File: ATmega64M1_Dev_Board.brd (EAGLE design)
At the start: 99.1 x 53.3 mm, 67 parts, among them IC1 LM1117IMPX-3.3, IC11 ATMEGA64M1TQFP32, IC2 LM1117IMPX-5.0, IC3 ADM3053M, IC4 FT232RL, J1 DCJ0202, Q1 16M, U1 MCP2562

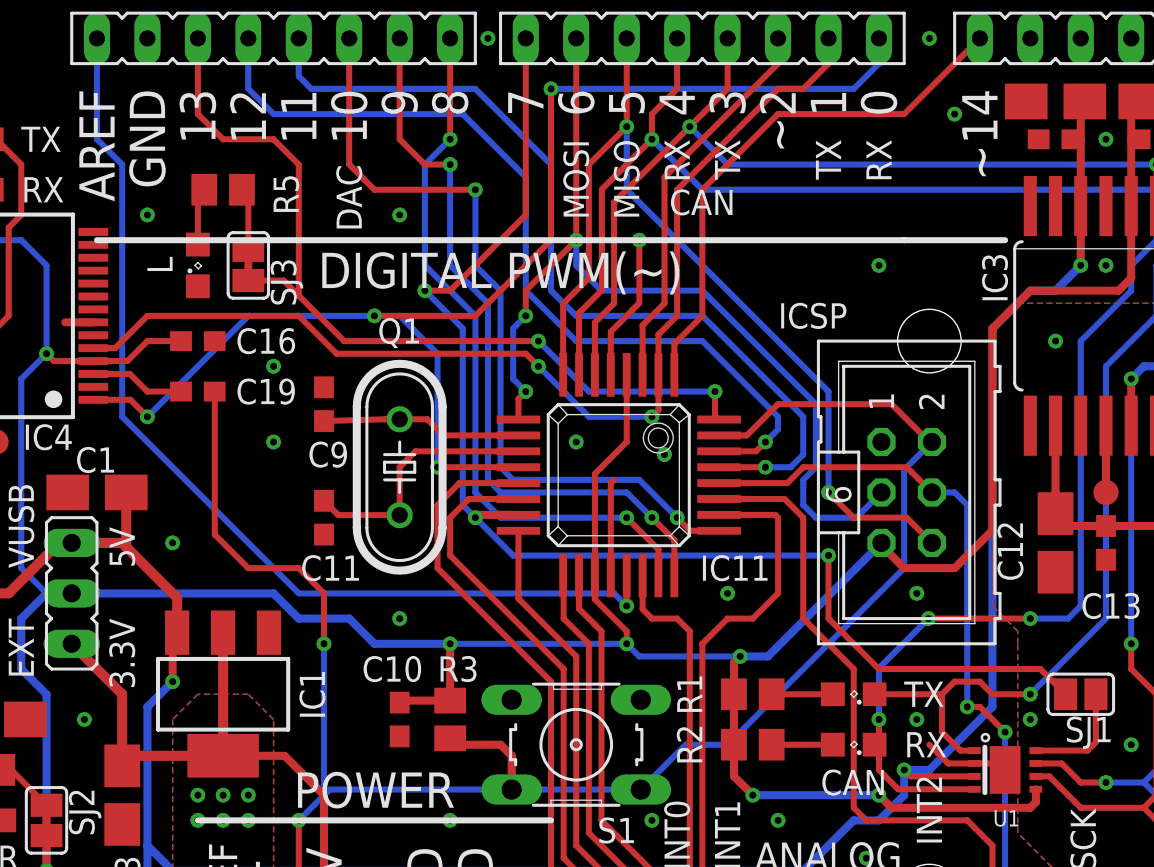
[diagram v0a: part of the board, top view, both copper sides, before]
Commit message: Fixed ICSP pin allocation.
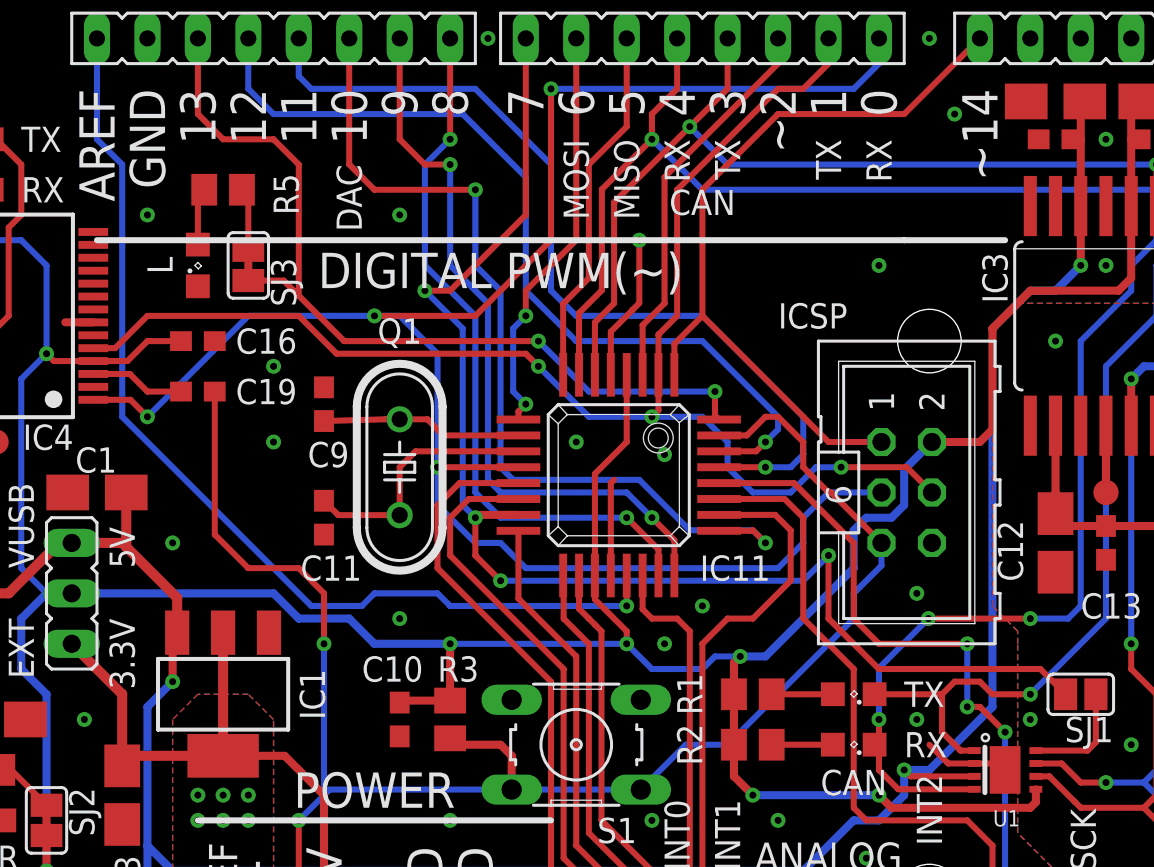
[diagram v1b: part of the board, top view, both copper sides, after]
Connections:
- net A8: no longer SV1.4
- net D0_RX: now also SV1.3
- net D14: now also SV1.1
- net D1_TX: now also SV1.4
- net D5: no longer SV1.6
- net D6: no longer SV1.3
- net GND: now also SV1.6; no longer SV1.1
- net RST: now also SV1.5; no longer SV1.2
- net VCC: now also SV1.2; no longer SV1.5
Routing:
- net D5: track 47.1 -> 18.3 mm, vias 2 -> 0
- net D0_RX: track 66.8 -> 94.7 mm
- net D6: track 47.2 -> 20.9 mm, vias 3 -> 2
- net D1_TX: track 54.4 -> 71.8 mm, vias 2 -> 3
- net D14: track 27.0 -> 38.7 mm
- net RST: track 93.5 -> 87.1 mm
- net D10: track 40.0 -> 45.2 mm
- net A8: track 42.6 -> 40.1 mm, vias 3 -> 4
- net D7: track 65.5 -> 67.7 mm, vias 3 -> 4
- net VCC: track 182.3 -> 180.9 mm
- net AREF: track 50.5 -> 51.0 mm
- net A6: track 37.6 -> 38.1 mm
- net GND: vias 32 -> 33
